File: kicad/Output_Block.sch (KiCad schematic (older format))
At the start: 88 parts, among them J601 ACJS-MHDRM, J602 ACJS-MHDRM, U601 NJM4558M, U602 NJM4558M, U603 ADG619BRMZ, U604 AD5263BRU200, U605 ADG619BRMZ, U606 NJM4558M, U607 NJM4558M, U608 AD5282BRUZ200

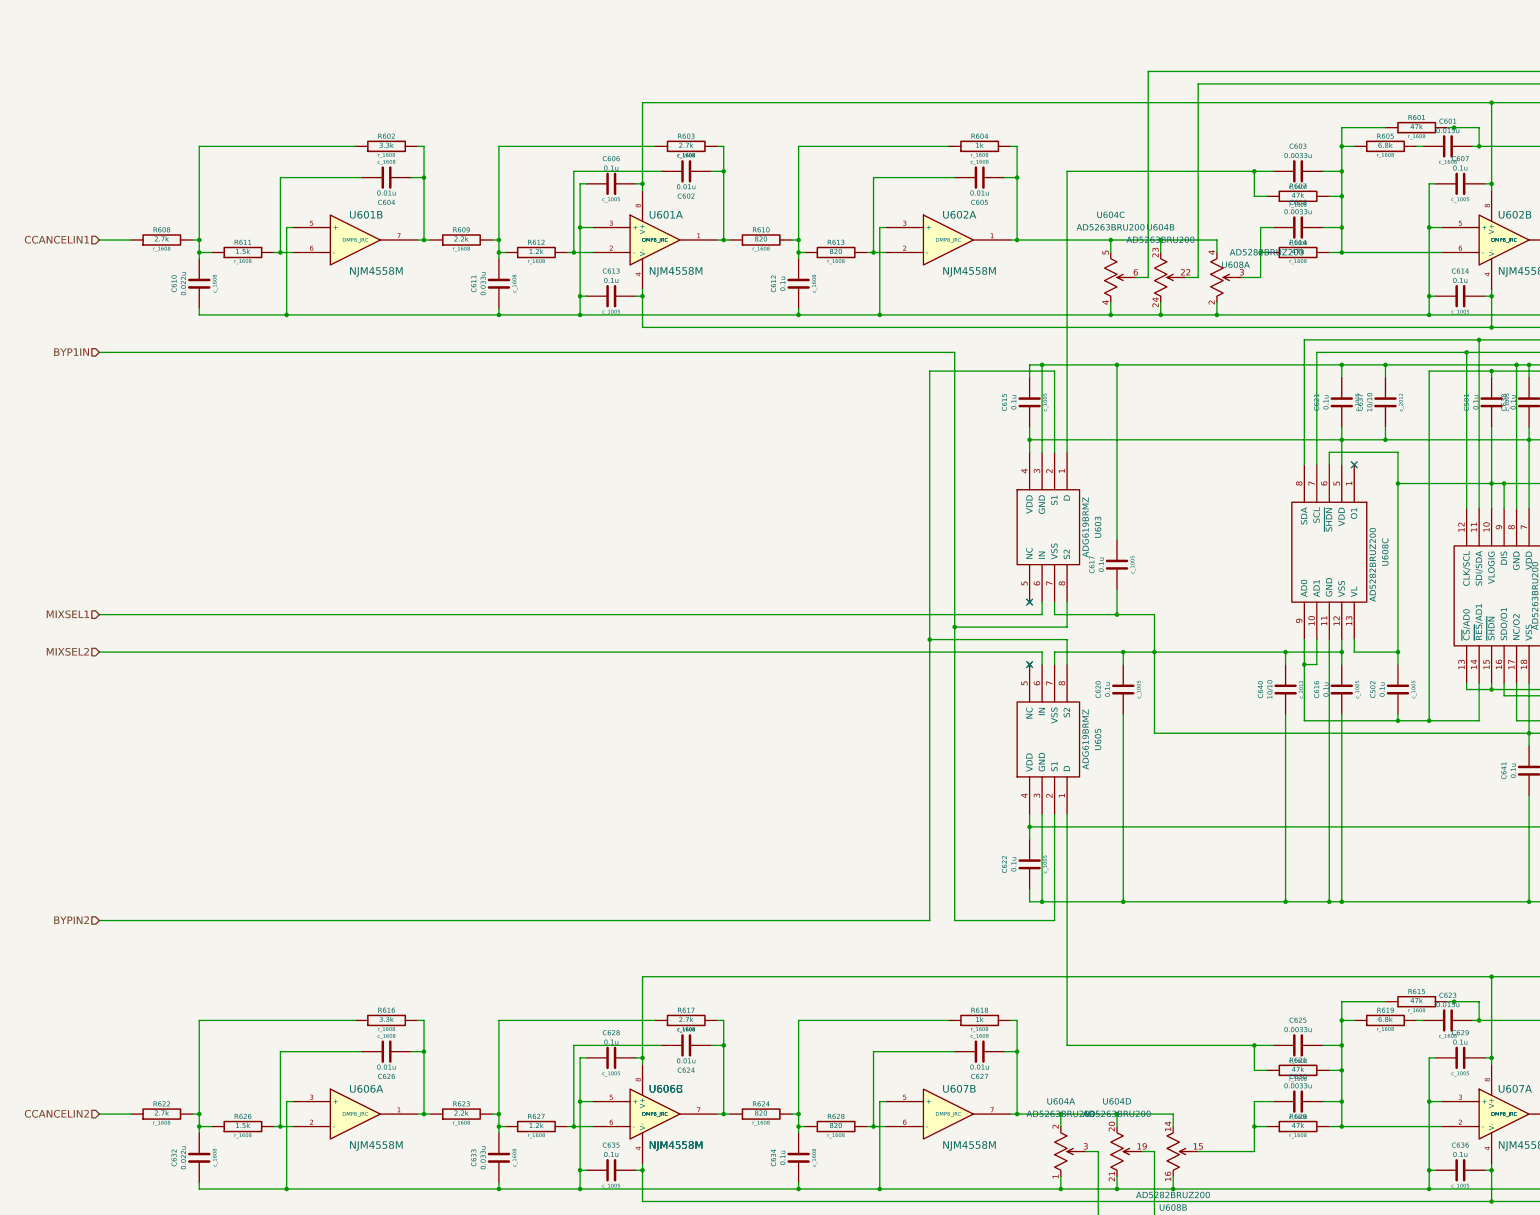
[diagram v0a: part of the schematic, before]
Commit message: Add: compander sch&pcb mod: constants
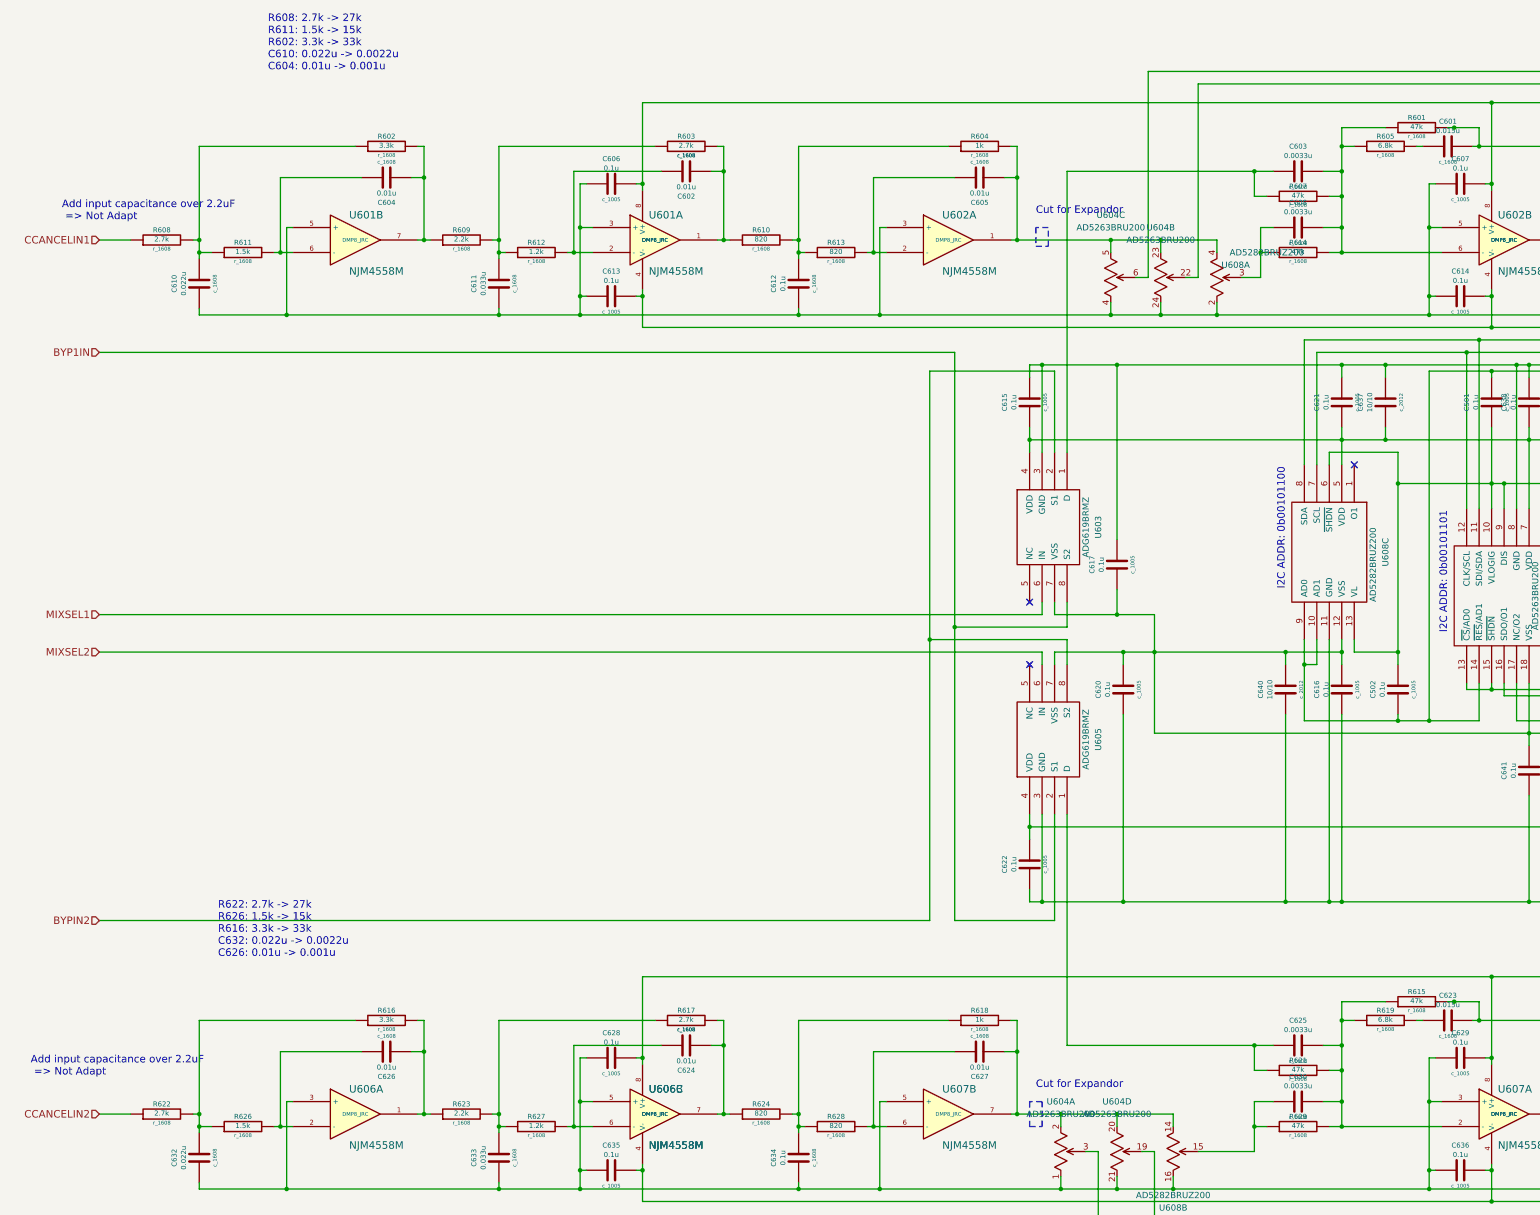
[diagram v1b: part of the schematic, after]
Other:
- note added: "Add input capacitance over 2.2uF\n => Not Adapt"
- note added: "Cut for Expandor"
- note added: "I2C ADDR: 0b00101100"
- note added: "I2C ADDR: 0b00101101"
- note added: "R608: 2.7k -> 27k\nR611: 1.5k -> 15k\nR602: 3.3k -> 33k\nC610: 0.022u -> 0.0022u\nC604: 0.01u -> 0.001u"
- note added: "R622: 2.7k -> 27k\nR626: 1.5k -> 15k\nR616: 3.3k -> 33k\nC632: 0.022u -> 0.0022u\nC626: 0.01u -> 0.001u"
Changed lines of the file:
@@
 LIBS:jrc
 LIBS:rohm
+LIBS:temp
+LIBS:alps
+LIBS:on_semiconductor
 LIBS:AnalogDelay-cache
 EELAYER 27 0
@@
 Sheet 5 6
 Title ""
-Date "15 dec 2013"
+Date "30 apr 2014"
 Rev ""
 Comp ""
@@
 Wire Wire Line
 	13550 6350 14700 6350
+Text Notes 11950 5650 1    60   ~ 0
+I2C ADDR: 0b00101101
+Text Notes 10650 5300 1    60   ~ 0
+I2C ADDR: 0b00101100
+Text Notes 600  9200 0    60   ~ 0
+Add input capacitance over 2.2uF\n => Not Adapt
+Text Notes 850  2350 0    60   ~ 0
+Add input capacitance over 2.2uF\n => Not Adapt
+Wire Notes Line
+	8650 2400 8650 2550
+Wire Notes Line
+	8650 2550 8750 2550
+Wire Notes Line
+	8750 2550 8750 2400
+Wire Notes Line
+	8750 2400 8650 2400
+Wire Notes Line
+	8600 9400 8600 9600
+Wire Notes Line
+	8600 9600 8700 9600
+Wire Notes Line
+	8700 9600 8700 9400
+Wire Notes Line
+	8700 9400 8600 9400
+Text Notes 8650 9300 0    60   ~ 0
+Cut for Expandor
+Text Notes 8650 2300 0    60   ~ 0
+Cut for Expandor
+Text Notes 2500 1150 0    60   ~ 0
+R608: 2.7k -> 27k\nR611: 1.5k -> 15k\nR602: 3.3k -> 33k\nC610: 0.022u -> 0.0022u\nC604: 0.01u -> 0.001u
+Text Notes 2100 8250 0    60   ~ 0
+R622: 2.7k -> 27k\nR626: 1.5k -> 15k\nR616: 3.3k -> 33k\nC632: 0.022u -> 0.0022u\nC626: 0.01u -> 0.001u
 $EndSCHEMATC

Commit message: mod: Schematics
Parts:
- C604, C626: value 0.01u -> 0.001u
- C610, C632: value 0.022u -> 0.0022u
- R602, R616: value 3.3k -> 33k
- R608, R622: value 2.7k -> 27k
- R611, R626: value 1.5k -> 15k
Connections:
- net expander/IN1_1: now reaches C605.1, R604.2, U602.1
- net expander/IN1_1: no longer U604.23 (A2), U604.5 (A3), U608.4 (B1)
- net expander/IN2_1: now reaches C627.1, R618.2, U607.7
- net expander/IN2_1: no longer U604.2 (A1), U604.20 (A4), U608.14 (B1)
- new net expander/OUT1: U604.23 (A2), U604.5 (A3), U608.4 (B1)
- new net expander/OUT2: U604.2 (A1), U604.20 (A4), U608.14 (B1)
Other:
- note removed: "Add input capacitance over 2.2uF\n => Not Adapt"
- note removed: "R608: 2.7k -> 27k\nR611: 1.5k -> 15k\nR602: 3.3k -> 33k\nC610: 0.022u -> 0.0022u\nC604: 0.01u -> 0.001u"
- note removed: "R622: 2.7k -> 27k\nR626: 1.5k -> 15k\nR616: 3.3k -> 33k\nC632: 0.022u -> 0.0022u\nC626: 0.01u -> 0.001u"
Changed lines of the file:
@@
 LIBS:jrc
 LIBS:rohm
-LIBS:temp
 LIBS:alps
 LIBS:on_semiconductor
@@
 $Descr A3 16535 11693
 encoding utf-8
-Sheet 5 6
+Sheet 6 8
 Title ""
-Date "30 apr 2014"
+Date "8 jun 2014"
 Rev ""
 Comp ""
@@
 P 3450 9000
 F 0 "C626" H 3450 9200 40  0000 C CNN
-F 1 "0.01u" H 3450 9125 40  0000 C CNN
+F 1 "0.001u" H 3450 9125 40  0000 C CNN
 F 2 "c_1608" H 3450 8875 30  0000 C CNN
 F 3 "~" V 3450 9000 60  0000 C CNN
@@
 P 1950 9850
 F 0 "C632" H 1950 10050 40  0000 C CNN
-F 1 "0.022u" H 1950 9975 40  0000 C CNN
+F 1 "0.0022u" H 1950 9975 40  0000 C CNN
 F 2 "c_1608" H 1950 9725 30  0000 C CNN
 F 3 "~" V 1950 9850 60  0000 C CNN
@@
 P 3450 8750
 F 0 "R616" V 3530 8750 40  0000 C CNN
-F 1 "3.3k" V 3457 8751 40  0000 C CNN
+F 1 "33k" V 3457 8751 40  0000 C CNN
 F 2 "r_1608" V 3380 8750 30  0000 C CNN
 F 3 "~" H 3450 8750 30  0000 C CNN
@@
 P 2300 9600
 F 0 "R626" V 2380 9600 40  0000 C CNN
-F 1 "1.5k" V 2307 9601 40  0000 C CNN
+F 1 "15k" V 2307 9601 40  0000 C CNN
 F 2 "r_1608" V 2230 9600 30  0000 C CNN
 F 3 "~" H 2300 9600 30  0000 C CNN
@@
 P 1650 9500
 F 0 "R622" V 1730 9500 40  0000 C CNN
-F 1 "2.7k" V 1657 9501 40  0000 C CNN
+F 1 "27k" V 1657 9501 40  0000 C CNN
 F 2 "r_1608" V 1580 9500 30  0000 C CNN
 F 3 "~" H 1650 9500 30  0000 C CNN
@@
 P 1950 2850
 F 0 "C610" H 1950 3050 40  0000 C CNN
-F 1 "0.022u" H 1950 2975 40  0000 C CNN
+F 1 "0.0022u" H 1950 2975 40  0000 C CNN
 F 2 "c_1608" H 1950 2725 30  0000 C CNN
 F 3 "~" V 1950 2850 60  0000 C CNN
@@
 P 3450 2000
 F 0 "C604" H 3450 2200 40  0000 C CNN
-F 1 "0.01u" H 3450 2125 40  0000 C CNN
+F 1 "0.001u" H 3450 2125 40  0000 C CNN
 F 2 "c_1608" H 3450 1875 30  0000 C CNN
 F 3 "~" V 3450 2000 60  0000 C CNN
@@
 P 1650 2500
 F 0 "R608" V 1730 2500 40  0000 C CNN
-F 1 "2.7k" V 1657 2501 40  0000 C CNN
+F 1 "27k" V 1657 2501 40  0000 C CNN
 F 2 "r_1608" V 1580 2500 30  0000 C CNN
 F 3 "~" H 1650 2500 30  0000 C CNN
@@
 P 3450 1750
 F 0 "R602" V 3530 1750 40  0000 C CNN
-F 1 "3.3k" V 3457 1751 40  0000 C CNN
+F 1 "33k" V 3457 1751 40  0000 C CNN
 F 2 "r_1608" V 3380 1750 30  0000 C CNN
 F 3 "~" H 3450 1750 30  0000 C CNN
@@
 P 2300 2600
 F 0 "R611" V 2380 2600 40  0000 C CNN
-F 1 "1.5k" V 2307 2601 40  0000 C CNN
+F 1 "15k" V 2307 2601 40  0000 C CNN
 F 2 "r_1608" V 2230 2600 30  0000 C CNN
 F 3 "~" H 2300 2600 30  0000 C CNN
@@
 Connection ~ 8850 9500
 Wire Wire Line
-	8850 9500 8850 9600
+	8850 8050 8850 9600
 Wire Wire Line
 	9600 9800 9600 10400
@@
 	8400 9000 8500 9000
 Wire Wire Line
-	8450 9500 9750 9500
+	8450 9500 8700 9500
+Wire Wire Line
+	8850 9500 9750 9500
 Wire Wire Line
 	8500 8750 8500 9500
@@
 	8400 2000 8500 2000
 Wire Wire Line
-	8450 2500 10100 2500
-Wire Wire Line
-	8500 1750 8500 2500
+	8500 2500 8450 2500
+Wire Wire Line
+	8800 2500 10100 2500
+Wire Wire Line
+	8500 1750 8500 3650
 Wire Wire Line
 	8450 1750 8500 1750
@@
 Text Notes 10650 5300 1    60   ~ 0
 I2C ADDR: 0b00101100
-Text Notes 600  9200 0    60   ~ 0
-Add input capacitance over 2.2uF\n => Not Adapt
-Text Notes 850  2350 0    60   ~ 0
-Add input capacitance over 2.2uF\n => Not Adapt
-Wire Notes Line
-	8650 2400 8650 2550
-Wire Notes Line
-	8650 2550 8750 2550
-Wire Notes Line
-	8750 2550 8750 2400
-Wire Notes Line
-	8750 2400 8650 2400
-Wire Notes Line
-	8600 9400 8600 9600
-Wire Notes Line
-	8600 9600 8700 9600
-Wire Notes Line
-	8700 9600 8700 9400
-Wire Notes Line
-	8700 9400 8600 9400
-Text Notes 8650 9300 0    60   ~ 0
-Cut for Expandor
 Text Notes 8650 2300 0    60   ~ 0
 Cut for Expandor
-Text Notes 2500 1150 0    60   ~ 0
-R608: 2.7k -> 27k\nR611: 1.5k -> 15k\nR602: 3.3k -> 33k\nC610: 0.022u -> 0.0022u\nC604: 0.01u -> 0.001u
-Text Notes 2100 8250 0    60   ~ 0
-R622: 2.7k -> 27k\nR626: 1.5k -> 15k\nR616: 3.3k -> 33k\nC632: 0.022u -> 0.0022u\nC626: 0.01u -> 0.001u
+$Sheet
+S 5600 3750 950  1050
+U 53946925
+F0 "expander" 50
+F1 "compander.sch" 50
+F2 "VOUT" O R 6550 3850 60
+F3 "OUT1" O R 6550 4000 60
+F4 "GND" U L 5600 4700 60
+F5 "IN1_3" I L 5600 4200 60
+F6 "IN1_2" I L 5600 4100 60
+F7 "IN1_1" I L 5600 4000 60
+F8 "VIN" I L 5600 3850 60
+F9 "OUT2" O R 6550 4350 60
+F10 "IN2_3" I L 5600 4550 60
+F11 "IN2_2" I L 5600 4450 60
+F12 "IN2_1" I L 5600 4350 60
+$EndSheet
+Wire Wire Line
+	8800 2500 8800 3300
+Wire Wire Line
+	8800 3300 7450 3300
+Wire Wire Line
+	7450 3300 7450 4000
+Wire Wire Line
+	7450 4000 6550 4000
+Wire Wire Line
+	8500 3650 5400 3650
+Wire Wire Line
+	5400 3650 5400 4000
+Wire Wire Line
+	5400 4000 5600 4000
+Wire Wire Line
+	8850 8050 7450 8050
+Wire Wire Line
+	7450 8050 7450 4350
+Wire Wire Line
+	7450 4350 6550 4350
+Wire Wire Line
+	5600 4350 5400 4350
+Wire Wire Line
+	5400 4350 5400 5050
+Wire Wire Line
+	5400 5050 7300 5050
+Wire Wire Line
+	7300 5050 7300 8150
+Wire Wire Line
+	7300 8150 8700 8150
+Wire Wire Line
+	8700 8150 8700 9500
+Wire Wire Line
+	5600 4700 4750 4700
+Wire Wire Line
+	4750 4700 4750 3100
+Connection ~ 4750 3100
 $EndSCHEMATC
